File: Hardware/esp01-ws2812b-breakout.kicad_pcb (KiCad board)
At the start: 2 copper layers, 37.8 x 23 mm, 21 parts, among them J1 Screw_Terminal_01x02, J2 Screw_Terminal_01x04, J3 Conn_01x03_Male, Q1 IRFS4127, Q2 IRFS4127, U1 LM1117-3.3, U2 ESP-01v090, U3 DS18B20

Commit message: Started re-doing the PCB layout
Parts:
- removed Q2: IRFS4127, Custom Mosfets:SOT-23_DS-REVERSED
- removed R4: 10K, Resistor_SMD:R_0805_2012Metric_Pad1.20x1.40mm_HandSolder
- J2: value Screw_Terminal_01x04 -> Screw_Terminal_01x03; footprint Custom Terminals:0104-blue-terminal -> custom_terminals:0103-blue-terminal
- R3: value 10K -> 470
- moved R2 9.84 mm to (166.1, 105.0)
- moved R1 9.29 mm to (162.3, 103.9)
- moved R3 4.11 mm to (171.2, 104.4)
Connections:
- J2 pad 3: LED2_5V -> GND
- Q1 pad 2: LED1_5V -> Net-(Q1-Pad2)
- R2 pad 2: LED1_5V -> Net-(Q1-Pad2)
- R3 pad 1: +3V3 -> LED1_5V
- R3 pad 2: LED2_3V3 -> Net-(Q1-Pad2)
- U2 pad 1: LED1_3V3 -> (no net)
- U2 pad 5: Net-(U2-Pad5) -> (no net)
- U2 pad 8: LED2_3V3 -> LED1_3V3
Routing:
- net DALLAS: track 60.2 -> 0.00 mm
- net +5V: track 69.6 -> 17.6 mm, vias 4 -> 1
- net LED2_5V: track 24.2 -> 0.00 mm, vias 2 -> 0
- net LED2_3V3: track 22.3 -> 0.00 mm, vias 2 -> 0
- net +3V3: track 88.9 -> 73.5 mm, vias 2 -> 1
- net GND: track 52.5 -> 45.4 mm, vias 6 -> 5
- net LED1_5V: track 19.0 -> 17.0 mm
- net LED1_3V3: track 55.5 -> 53.6 mm, vias 3 -> 2

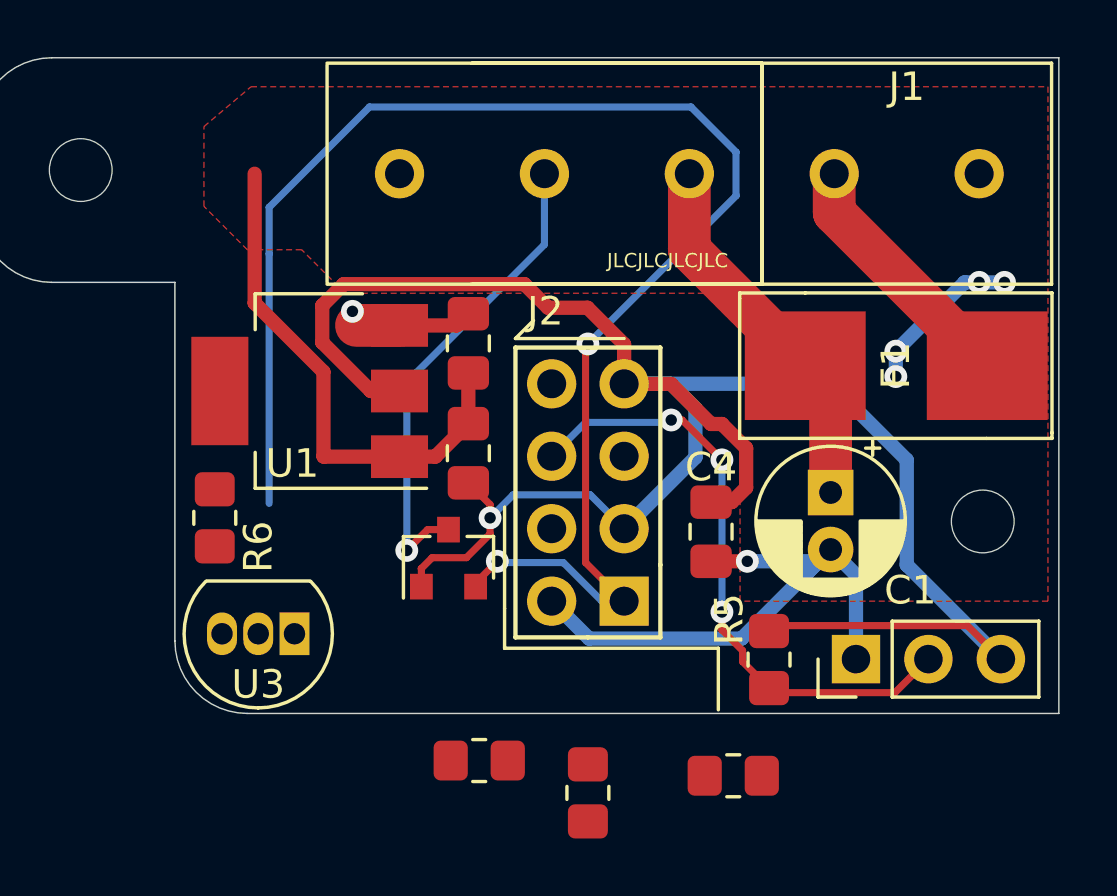
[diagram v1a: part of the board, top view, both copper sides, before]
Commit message: Updated PCB layout, removed obsolete traces
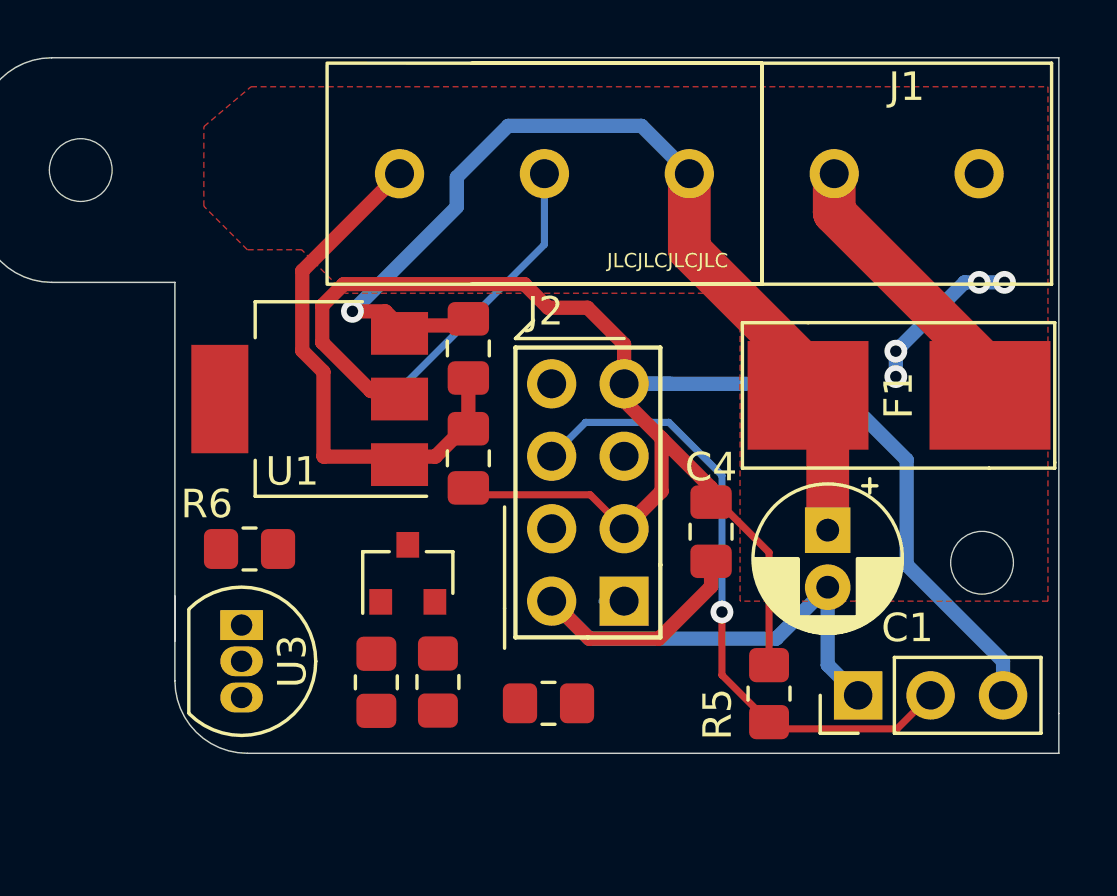
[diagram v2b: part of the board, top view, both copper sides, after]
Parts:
- moved R3 6.96 mm to (164.7, 101.9)
- moved R2 6.54 mm to (160.9, 101.1)
- moved R1 4.53 mm to (158.7, 101.1), turned to 270 degrees
- moved U3 1.88 mm to (154.0, 99.1), turned to 270 degrees
- moved R6 1.64 mm to (154.3, 96.5), turned to 0 degrees
- moved Q1 1.52 mm to (159.8, 97.3)
- moved H2 1.45 mm to (179.9, 97.0)
- moved C1 1.32 mm to (174.5, 95.8)
- moved J3 1.27 mm to (175.6, 101.6)
- moved R5 1.19 mm to (172.5, 101.5)
- moved F1 1.05 mm to (173.8, 91.1)
- moved U1 0.28 mm to (156.4, 91.2)
- moved C3 0.18 mm to (161.9, 93.3)
- moved C2 0.18 mm to (161.9, 89.4)
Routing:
- net LED1_3V3: track 53.6 -> 0.00 mm, vias 2 -> 0
- net +5V: track 17.6 -> 36.1 mm
- net +3V3: track 73.5 -> 62.5 mm, vias 1 -> 0
- net LED1_5V: track 17.0 -> 9.31 mm, vias 1 -> 0
- net GND: track 45.4 -> 47.6 mm, vias 5 -> 4
- net (no net): track 0.00 -> 0.78 mm
- net GPIO0: track 22.1 -> 22.8 mm, vias 3 -> 1
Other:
- board size 37.8 x 23 mm -> 37.8 x 24.4 mm

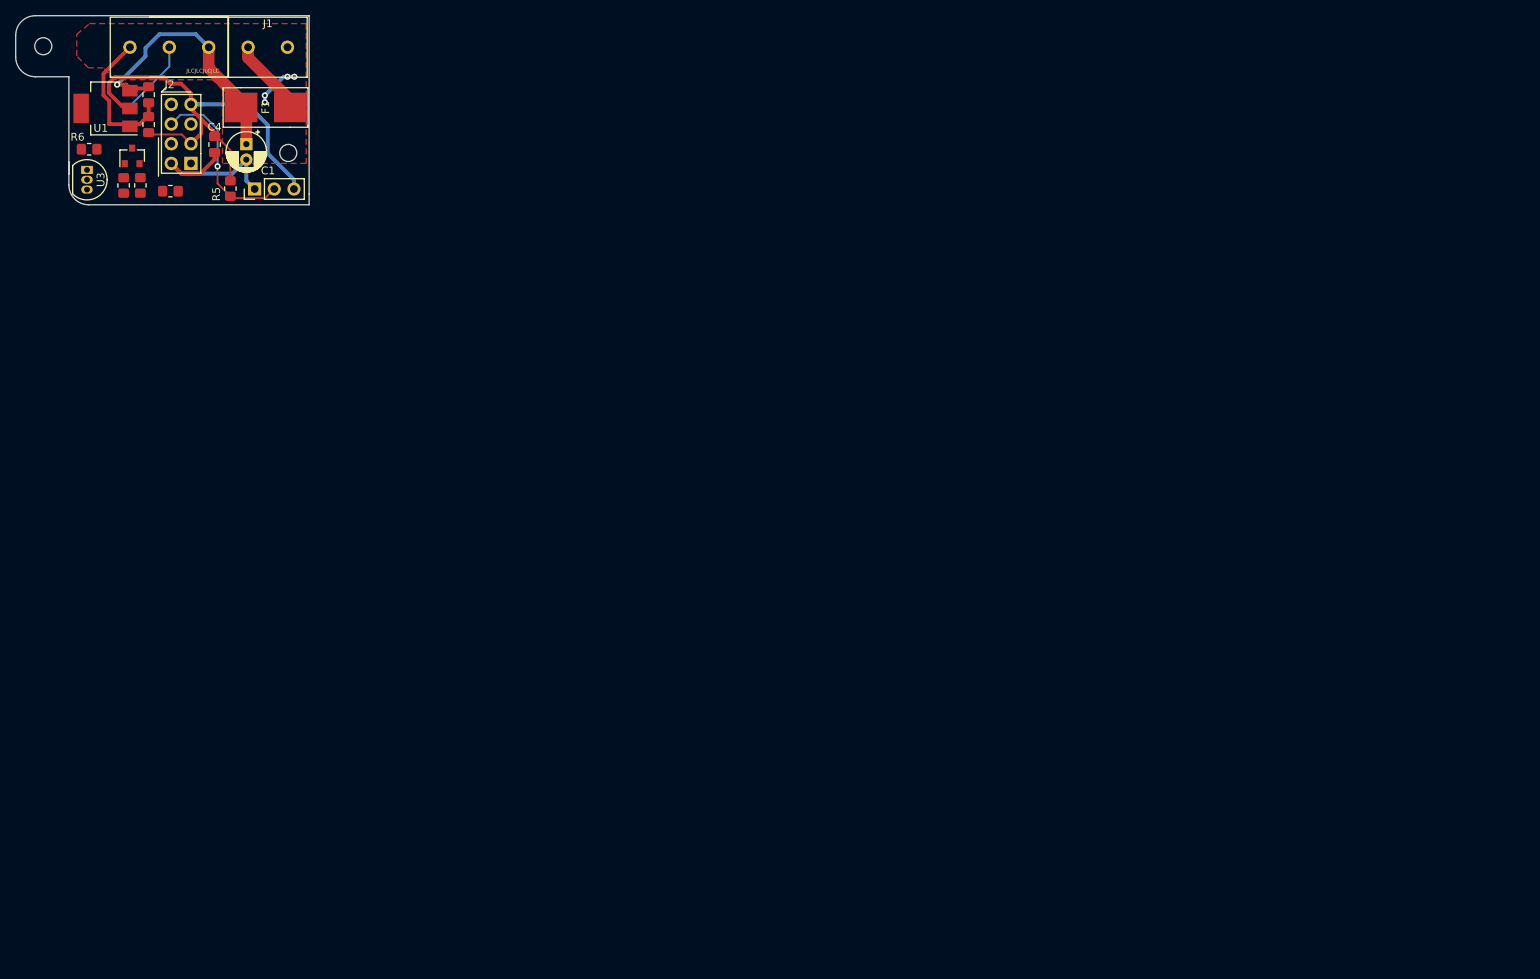
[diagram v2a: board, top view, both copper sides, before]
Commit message: Updated schematic export, finished PCB design
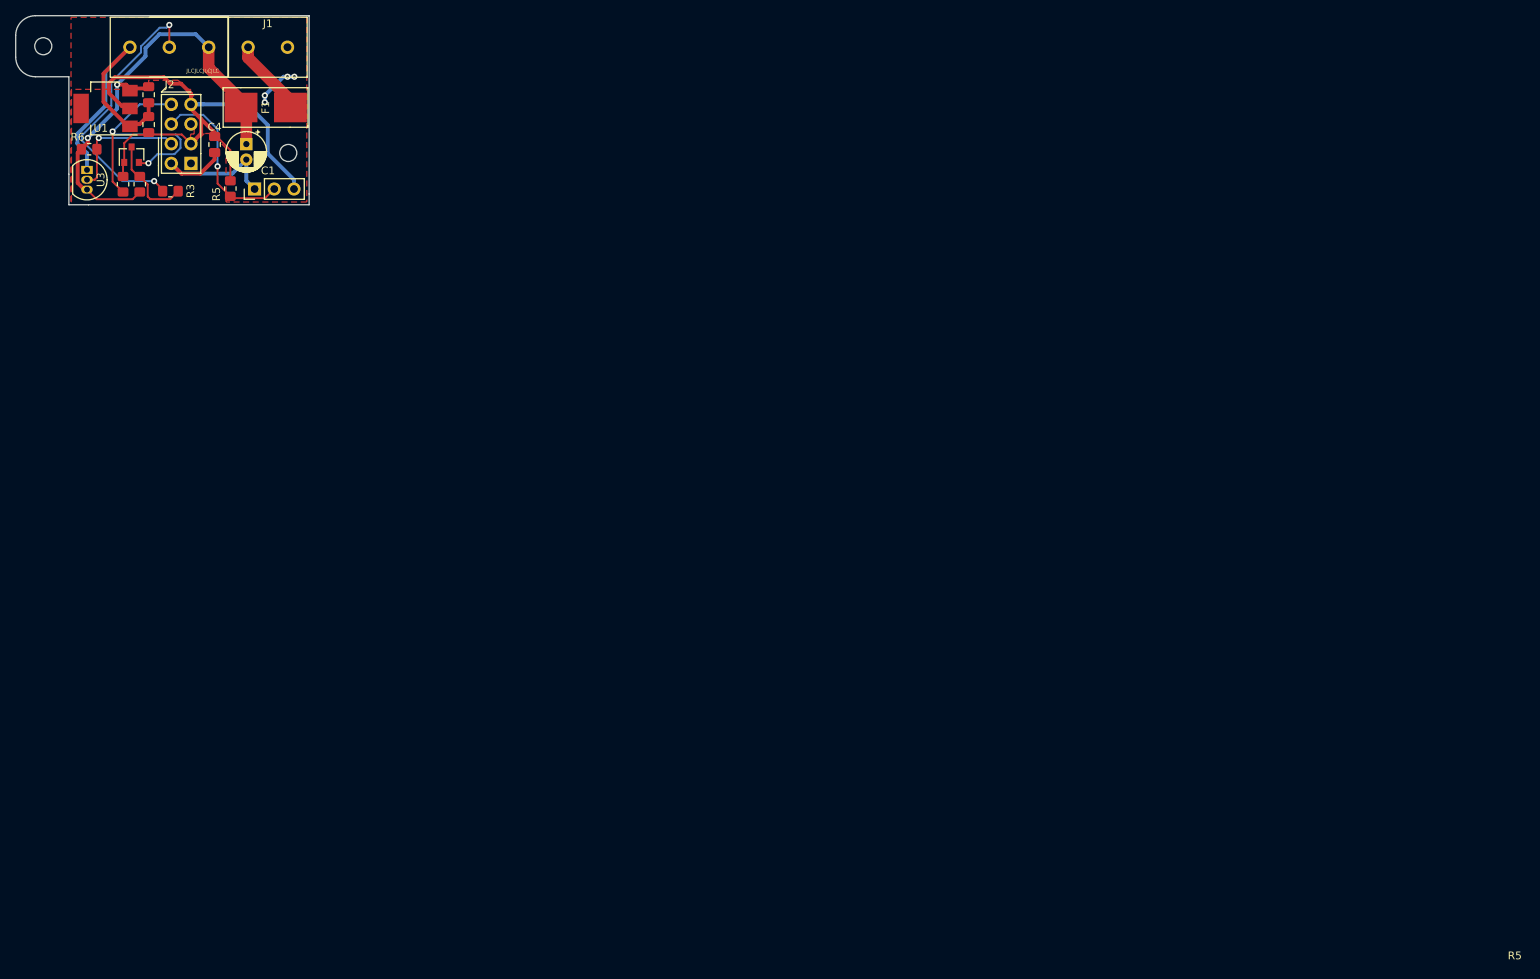
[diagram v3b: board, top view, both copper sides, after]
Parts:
- added ?: , , F.Cu at (170.1, 103.0)
- moved Q1 0.17 mm to (159.7, 97.2)
- moved R1 0.17 mm to (158.6, 101.0)
- moved R2 0.17 mm to (160.8, 101.0)
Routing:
- net LED1_3V3: track 0.00 -> 34.0 mm, vias 0 -> 2
- net LED1_5V: track 9.31 -> 36.2 mm, vias 0 -> 2
- net +5V: track 36.1 -> 60.1 mm, vias 1 -> 2
- net GND: track 47.6 -> 66.5 mm
- net DALLAS: track 0.00 -> 16.3 mm, vias 0 -> 1
- net Net-(Q1-Pad2): track 0.00 -> 11.9 mm
- net +3V3: track 62.5 -> 70.6 mm
- net (no net): track 0.78 -> 0.00 mm
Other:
- outline, holes or cut-outs redrawn
- board text added: "R3"

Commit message: Cosmetic tweaks
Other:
- board text added: "LED"
- board text removed: "LED1"
- board text removed: "LED2"
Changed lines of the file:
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@@
   (general
     (thickness 1.6)
-    (drawings 31)
+    (drawings 30)
     (tracks 155)
     (zones 0)
@@
   (module custom_terminals:0103-blue-terminal (layer F.Cu)
     (at 169.672 83.312 180)
-    (fp_text reference J2 (at 5.05 -4.825) (layer F.SilkS)
+    (fp_text reference J2 (at 5.2832 2.9464) (layer F.SilkS)
       (effects (font (size 1 1) (thickness 0.15)))
     )
@@
     (tags "CMS SOT")
     (attr smd)
-    (fp_text reference U1 (at 0.61 -2.54) (layer F.SilkS)
+    (fp_text reference U1 (at 3.327 -2.8702) (layer F.SilkS)
       (effects (font (size 1 1) (thickness 0.15)))
     )
@@
     (tags "capacitor handsolder")
     (attr smd)
-    (fp_text reference C4 (at 2.2645 0 180) (layer F.SilkS)
+    (fp_text reference C4 (at -2.6123 0 180) (layer F.SilkS)
       (effects (font (size 1 1) (thickness 0.15)))
     )
@@
   (module "Custom Fuses:1808_SMD_Fuse_Holder" (layer F.Cu)
     (at 173.833 91.0844)
-    (fp_text reference F1 (at 3.175 0 90) (layer F.SilkS)
+    (fp_text reference F1 (at -3.0434 -0.0254 90) (layer F.SilkS)
       (effects (font (size 1 1) (thickness 0.15)))
     )
@@
     (tags "resistor handsolder")
     (attr smd)
-    (fp_text reference R5 (at -0.7206 -1.8034 90) (layer F.SilkS)
+    (fp_text reference R5 (at 0.016 -1.5748 90) (layer F.SilkS)
       (effects (font (size 1 1) (thickness 0.15)))
     )
@@
     (tags "resistor handsolder")
     (attr smd)
-    (fp_text reference R6 (at -1.4986 -1.5748 180) (layer F.SilkS)
+    (fp_text reference R6 (at 2.5654 -0.0254 270) (layer F.SilkS)
       (effects (font (size 1 1) (thickness 0.15)))
     )
@@
   (gr_line (start 163.195 98.552) (end 163.195 94.996) (layer F.SilkS) (width 0.12))
   (gr_line (start 163.195 98.552) (end 163.195 99.949) (layer F.SilkS) (width 0.12))
-  (gr_line (start 151.892 84.709) (end 151.892 79.375) (layer B.SilkS) (width 0.12))
+  (gr_line (start 156.972 84.709) (end 156.972 79.375) (layer B.SilkS) (width 0.12))
   (gr_line (start 172.212 79.375) (end 172.212 84.709) (layer B.SilkS) (width 0.12))
   (gr_line (start 182.372 79.375) (end 182.372 84.709) (layer B.SilkS) (width 0.12))
-  (gr_text GND (at 154.432 81.661) (layer B.SilkS)
+  (gr_text GND (at 159.4612 81.5848) (layer B.SilkS)
     (effects (font (size 1 1) (thickness 0.15)) (justify mirror))
   )
-  (gr_text LED2 (at 159.512 81.661) (layer B.SilkS)
-    (effects (font (size 1 1) (thickness 0.15)) (justify mirror))
-  )
-  (gr_text LED1 (at 164.592 81.661) (layer B.SilkS)
+  (gr_text LED (at 164.592 81.661) (layer B.SilkS)
     (effects (font (size 1 1) (thickness 0.15)) (justify mirror))
   )
@@
     (effects (font (size 1 1) (thickness 0.15)) (justify mirror))
   )
-  (gr_text OUT (at 162.179 80.137) (layer B.SilkS)
+  (gr_text OUT (at 164.6174 80.2386) (layer B.SilkS)
     (effects (font (size 1 1) (thickness 0.15)) (justify mirror))
   )
-  (gr_text IN (at 177.292 80.137) (layer B.SilkS)
+  (gr_text IN (at 177.3428 80.1116) (layer B.SilkS)
     (effects (font (size 1 1) (thickness 0.15)) (justify mirror))
   )
-  (gr_line (start 172.212 84.709) (end 151.892 84.709) (layer B.SilkS) (width 0.12))
-  (gr_line (start 151.892 79.375) (end 172.212 79.375) (layer B.SilkS) (width 0.12))
+  (gr_line (start 172.212 84.709) (end 156.972 84.709) (layer B.SilkS) (width 0.12))
+  (gr_line (start 156.972 79.375) (end 172.212 79.375) (layer B.SilkS) (width 0.12))
   (gr_line (start 182.372 84.709) (end 172.212 84.709) (layer B.SilkS) (width 0.12))
   (gr_line (start 172.212 79.375) (end 182.372 79.375) (layer B.SilkS) (width 0.12))
@@
     (effects (font (size 0.5 0.5) (thickness 0.1)))
   )
-  (gr_text "ESP-01 5V Addressable RGB LED Breakout\n\nDeveloped by Arjan Buijserd" (at 167.386 86.995) (layer B.SilkS)
+  (gr_text "ESP-01 5V Addressable RGB LED Breakout\n\nDeveloped by Arjan Buijserd" (at 167.1066 87.2744) (layer B.SilkS)
     (effects (font (size 0.8 0.8) (thickness 0.153)) (justify mirror))
   )
